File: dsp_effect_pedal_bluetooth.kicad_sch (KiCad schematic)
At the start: 28 parts, among them J1 0022232041, J4 0022232041, Q3 2N5088BU_Obsolete, Q4 2N5088BU_Obsolete, U1 MCP6002-I_P, U11 MT3608

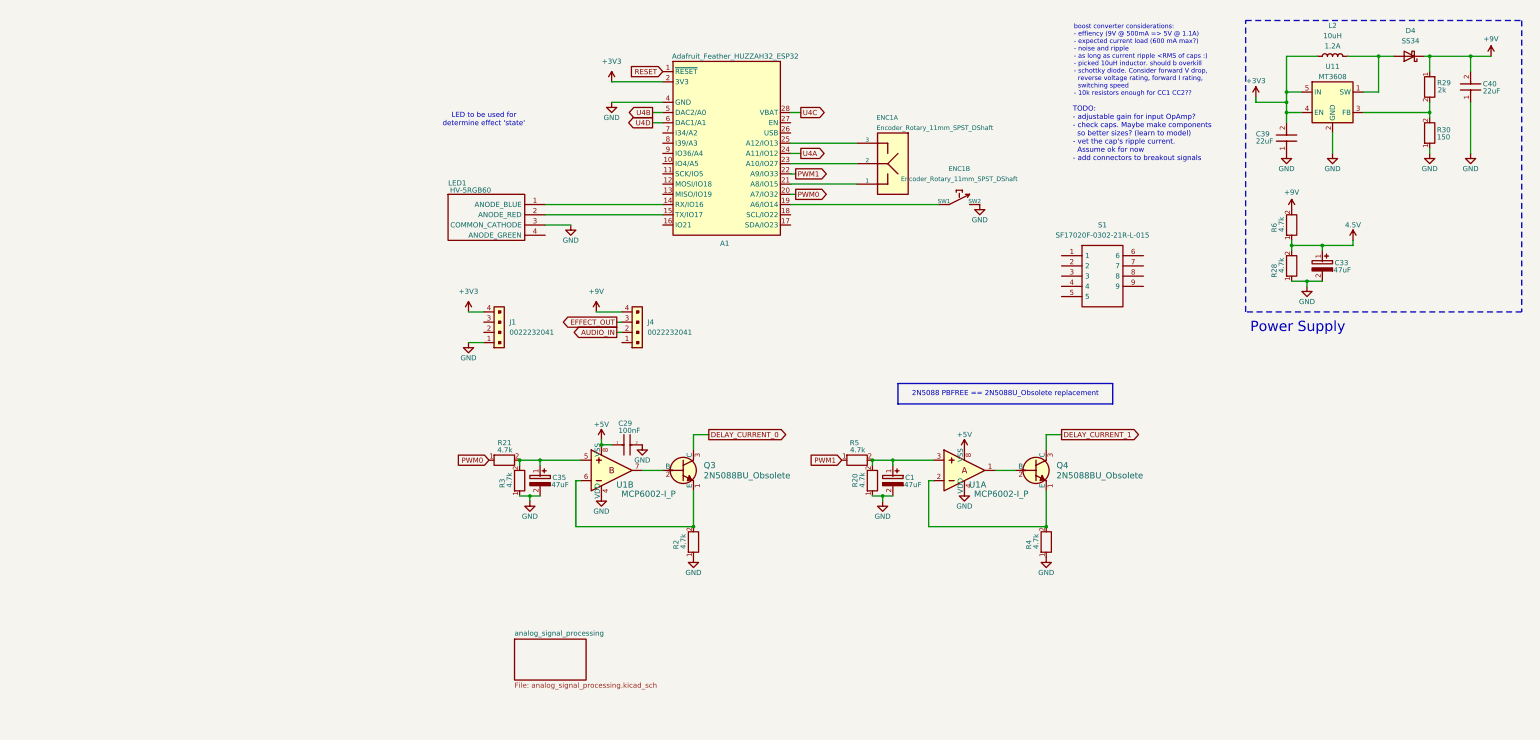
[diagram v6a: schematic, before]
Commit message: initial board routing
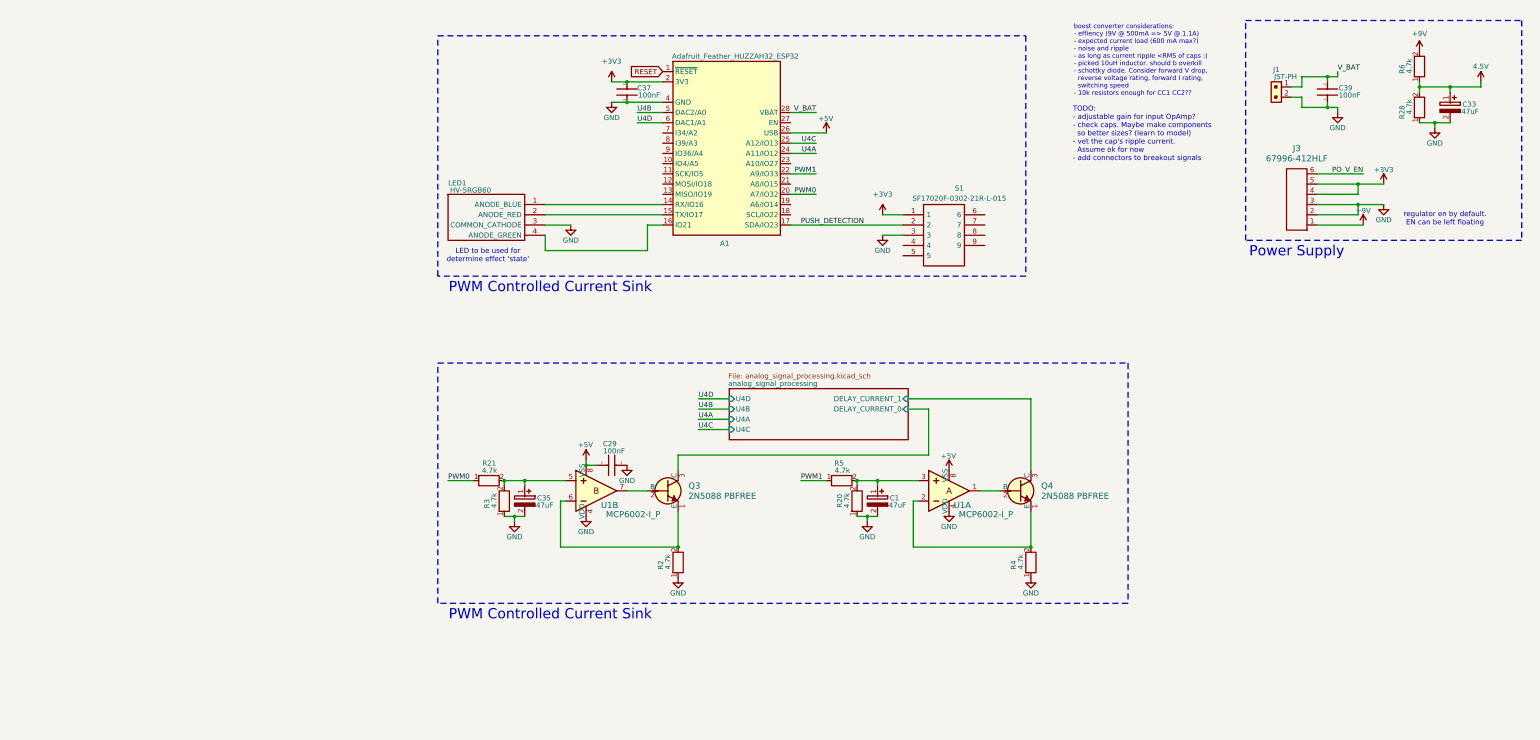
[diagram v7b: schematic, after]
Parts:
- removed C39, C40: 22uF, FG20, symbol SamacSys_Parts:FG20X7R1C226MRT06
- removed D4: SS34, Diode_SMD:D_SMA, symbol Diode:SS34
- removed ENC1: Encoder_Rotary_11mm_SPST_DShaft, 4ms_Encoder:ENC_SPST_12mm, symbol PCM_4ms_Switch:Encoder_Rotary_11mm_SPST_DShaft
- removed J1, J4: 0022232041, digikey-footprints:PinHeader_1x4_P2.54mm_Drill1.02mm, symbol dk_Rectangular-Connectors-Headers-Male-Pins:0022232041
- removed L2: 10uH_1.0A_4018, Inductor_SMD:L_Taiyo-Yuden_NR-40xx, symbol PCM_4ms_Inductor:10uH_1.0A_4018
- removed R29: 2k, RESAD1550W60L630D230, symbol SamacSys_Parts:YR1B2K0CC
- removed R30: 150, RESAD1590W60L630D240, symbol SamacSys_Parts:MFR-25FBF52-150R
- removed U11: MT3608, Package_TO_SOT_SMD:SOT-23-6, symbol Regulator_Switching:MT3608
- added C37, C39: 100nF, digikey-footprints:1206, symbol SamacSys_Parts:SR211C104KARTR1
- added J1: JST-PH, digikey-footprints:PinHeader_1x2_P2mm_Drill1mm, symbol dk_Rectangular-Connectors-Headers-Male-Pins:B2B-PH-K-S_LF__SN_
- added J3: 67996-412HLF, Connector_PinHeader_2.54mm:PinHeader_1x06_P2.54mm_Vertical, symbol dk_Rectangular-Connectors-Headers-Male-Pins:67996-412HLF
- C1, C33, C35: footprint CAPPRD200W50D525H1250 -> digikey-footprints:1206
- C29: footprint SR211C104KARTR1 -> digikey-footprints:1206
- Q3, Q4: value 2N5088BU_Obsolete -> 2N5088 PBFREE
- R2, R20, R21, R28, R3, R4, R5, R6: footprint RESAD1590W60L630D240 -> digikey-footprints:1206
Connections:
- net +3V3: now also S1.1, C37.2, J3.4, J3.5
- net +5V: now also A1.26 (USB)
- net +9V: now also J3.1
- net GND: now also S1.3, C37.1, C39.1, J1.2, J3.2, J3.3
- net U4C: now also A1.25 (A12/IO13); no longer A1.28 (VBAT)
- net at LED1.4 (ANODE_GREEN): now also A1.16 (IO21)
- net PUSH_DETECTION: now reaches S1.2
- net PUSH_DETECTION: now also A1.17 (SDA/IO23)
- net DELAY_CURRENT_0 renamed analog_signal_processing/DELAY_CURRENT_0
- net DELAY_CURRENT_1 renamed analog_signal_processing/DELAY_CURRENT_1
- new net PO_V_EN: J3.6
- new net V_BAT: A1.28 (VBAT), C39.2, J1.1
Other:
- sheet analog_signal_processing ports: added DELAY_CURRENT_0, DELAY_CURRENT_1, U4A, U4B, U4C, U4D; removed none
- note added: "PWM Controlled Current Sink"
- note added: "regulator en by default. EN can be left floating"
- note removed: "2N5088 PBFREE == 2N5088U_Obsolete replacement"
- moved on the sheet: C1, C29, C33, C35, Q3, Q4, R2, R20, R21, R28, R3, R4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
